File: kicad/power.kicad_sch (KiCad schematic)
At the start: 65 parts, among them J9 USB_C_Receptacle_USB2.0_16P, SW15 PH_IND, T1 475uH, U20 TPS7A39, U21 SN6505BDBV, U22 TPS2116DRL, U23 TPS62172DSG, U25 TPS7A2009, U26 TPS62171DSG, U27 TPS7A4101, U28 TPS61391, U29 CH224K

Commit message: layout updates
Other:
- note added: "power supply"
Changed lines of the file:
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@@
+		)
+	)
+	(text "power supply"
+		(exclude_from_sim no)
+		(at 352.806 245.872 0)
+		(effects
+			(font
+				(size 2.54 2.54)
+			)
+			(justify left bottom)
 		)
 	)

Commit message: #16
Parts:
- C172, C173: value 0.47uF -> 470nF
- C176: value 0.01uF -> 10nF
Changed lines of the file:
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@@
 			)
 		)
-		(property "Value" "0.47uF"
+		(property "Value" "470nF"
 			(at 105.41 204.4699 0)
 			(show_name no)
@@
 			)
 		)
-		(property "Value" "0.01uF"
+		(property "Value" "10nF"
 			(at 196.85 204.4699 0)
 			(show_name no)
@@
 			)
 		)
-		(property "Value" "0.47uF"
+		(property "Value" "470nF"
 			(at 91.44 204.4699 0)
 			(show_name no)

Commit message: power supply footprints
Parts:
- removed C164: 10uF, symbol Device:C
- removed D60, D61: D_Schottky, symbol Device:D_Schottky
- removed D62: 100V, symbol Device:D
- added D61: BAS316, Diode_SMD:D_SOD-323, symbol Diode:BAS316
- added D64, D69: MBR0580, Diode_SMD:D_SOD-123, symbol Diode:MBR0580
- C157, C158, C159, C160, C161, C162, C165, C166, C167, C168, C169, C170, C171, C172, C173, C174, C175, C176, C177, C178, C180, C197, C198: footprint (none) -> Capacitor_SMD:C_0805_2012Metric_Pad1.18x1.45mm_HandSolder
- C163: value 10uF -> 22uF; footprint (none) -> Capacitor_SMD:C_0805_2012Metric_Pad1.18x1.45mm_HandSolder
- C179: footprint (none) -> Capacitor_SMD:C_0603_1608Metric_Pad1.08x0.95mm_HandSolder
- D63: footprint (none) -> LED_SMD:LED_0603_1608Metric_Pad1.05x0.95mm_HandSolder
- R103, R104, R105, R106, R107, R108, R109, R112, R113, R114, R115, R118, R119, R120, R121, R122: footprint (none) -> Resistor_SMD:R_0805_2012Metric_Pad1.20x1.40mm_HandSolder
- R110: value 10k -> 330k; footprint (none) -> Resistor_SMD:R_0805_2012Metric_Pad1.20x1.40mm_HandSolder
- R111: value 10k -> 100k; footprint (none) -> Resistor_SMD:R_0805_2012Metric_Pad1.20x1.40mm_HandSolder
- R116, R117: footprint (none) -> Resistor_SMD:R_0603_1608Metric_Pad0.98x0.95mm_HandSolder
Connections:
- net at C172.1, C173.1, C174.1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: now also D61.1 (K)
- net at L3.2, U28.8 (SW): now also D61.2 (A)
- net at C162.2, U20.5 (INN): now also D69.2 (A)
- net at C158.1, R105.1, U20.1 (INP): now also D64.1 (K)
- net at T1.6: now also D64.2 (A), D69.1 (K)
- net GND1 renamed GNDA

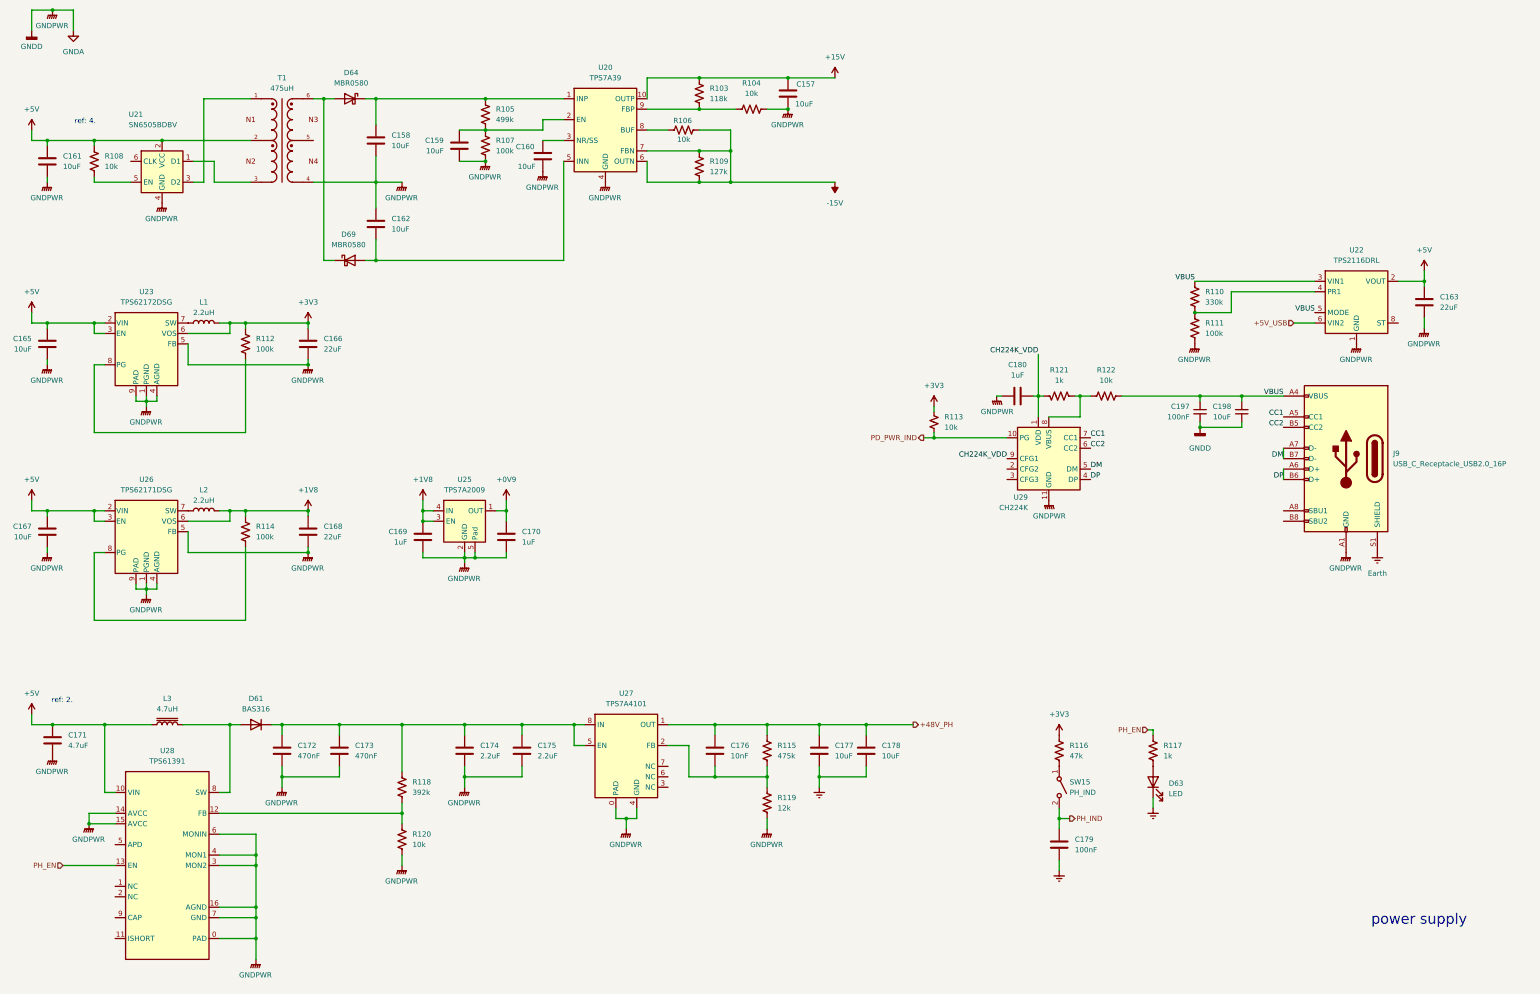
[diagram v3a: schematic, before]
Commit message: push buttons
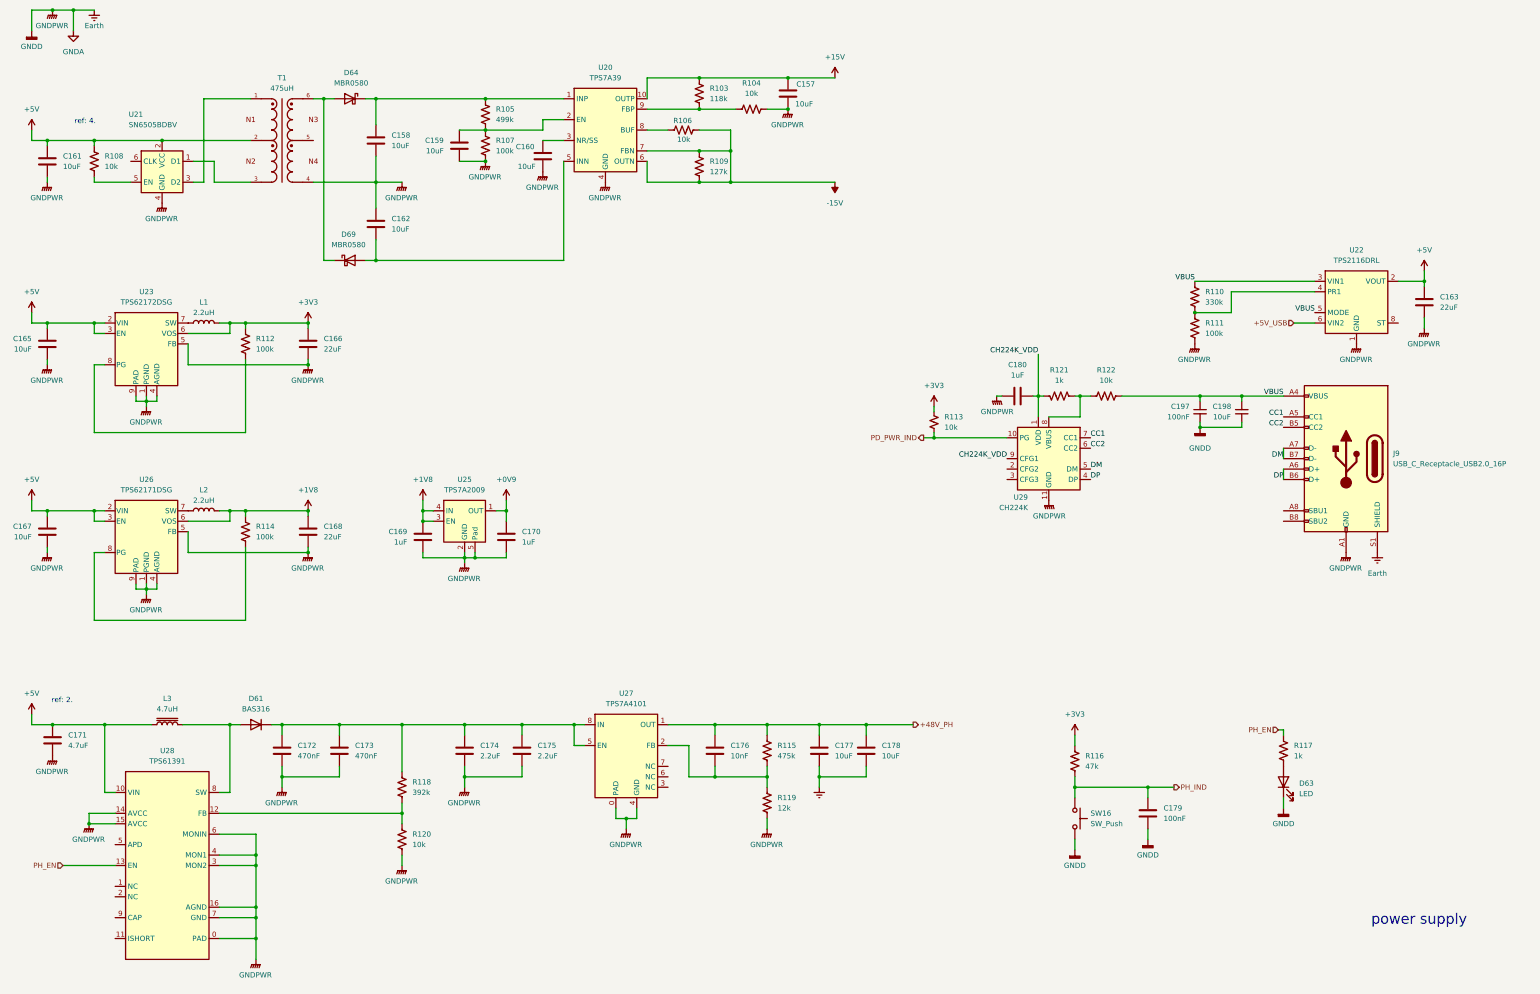
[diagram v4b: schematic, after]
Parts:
- removed SW15: PH_IND, symbol Switch:SW_SPST
- added SW16: SW_Push, Button_Switch_SMD:SW_Push_1P1T_XKB_TS-1187A, symbol Switch:SW_Push
- J9: footprint (none) -> Connector_USB:USB_C_Receptacle_HRO_TYPE-C-31-M-12
- T1: footprint WE-PPTI_1006:WE-PPTI_1006_L10.2W6.73H4.19 -> openmic:Wurth Elektronik 760390015
- U27: footprint (none) -> Package_SO:Texas_DGN0008B_VSSOP-8-1EP_3x3mm_P0.65mm_EP2x3mm_Mask1.88x1.98mm_ThermalVias
- U28: footprint (none) -> openmic:TPS61391
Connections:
- net GNDA is gone; now on net Earth: C157.2, C158.2, C159.2, C160.2, C161.2, C162.1, C163.2, C165.2, C166.2, C167.2, C168.2, C169.2, C170.2, C171.2, C172.2, C173.2, C174.2, C175.2, C180.2, C197.2, C198.1, J9.A1 (GND), J9.A12 (GND), J9.B1 (GND), J9.B12 (GND), R104.2, R107.2, R111.2, R119.2, R120.2, T1.4, U20.11 (GND), U20.4 (GND), U21.4 (GND), U22.1 (GND), U23.1 (PGND), U23.4 (AGND), U23.5 (FB), U23.9 (PAD), U25.2 (GND), U25.5 (Pad), U26.1 (PGND), U26.4 (AGND), U26.5 (FB), U26.9 (PAD), U27.0 (PAD), U27.4 (GND), U28.0 (PAD), U28.14 (AVCC), U28.15 (AVCC), U28.16 (AGND), U28.3 (MON2), U28.4 (MON1), U28.6 (MONIN), U28.7 (GND), U29.11 (GND)
- net Earth: now also SW16.2
- net PH_IND: now also R116.2, SW16.1
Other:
- moved on the sheet: D63, R117

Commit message: footprint selection
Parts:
- L1, L2, L3: footprint (none) -> Inductor_SMD:L_Wuerth_PMCI-201610
- R113: footprint Resistor_SMD:R_0805_2012Metric_Pad1.20x1.40mm_HandSolder -> Resistor_SMD:R_0603_1608Metric_Pad0.98x0.95mm_HandSolder

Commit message: footprints
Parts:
- U28: footprint openmic:TPS61391 -> Package_DFN_QFN:WQFN-16-1EP_3x3mm_P0.5mm_EP1.6x1.6mm
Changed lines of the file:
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@@
 			)
 		)
-		(property "Footprint" "openmic:TPS61391"
+		(property "Footprint" "Package_DFN_QFN:WQFN-16-1EP_3x3mm_P0.5mm_EP1.6x1.6mm"
 			(at 59.69 231.14 0)
 			(hide yes)

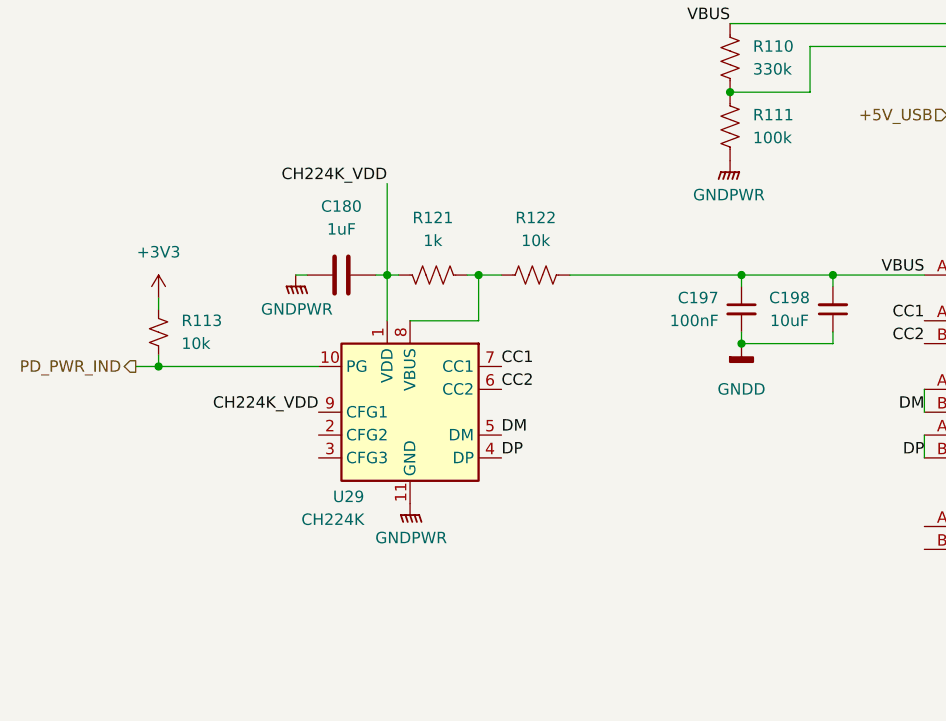
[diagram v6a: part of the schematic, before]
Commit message: update ch224k vdd
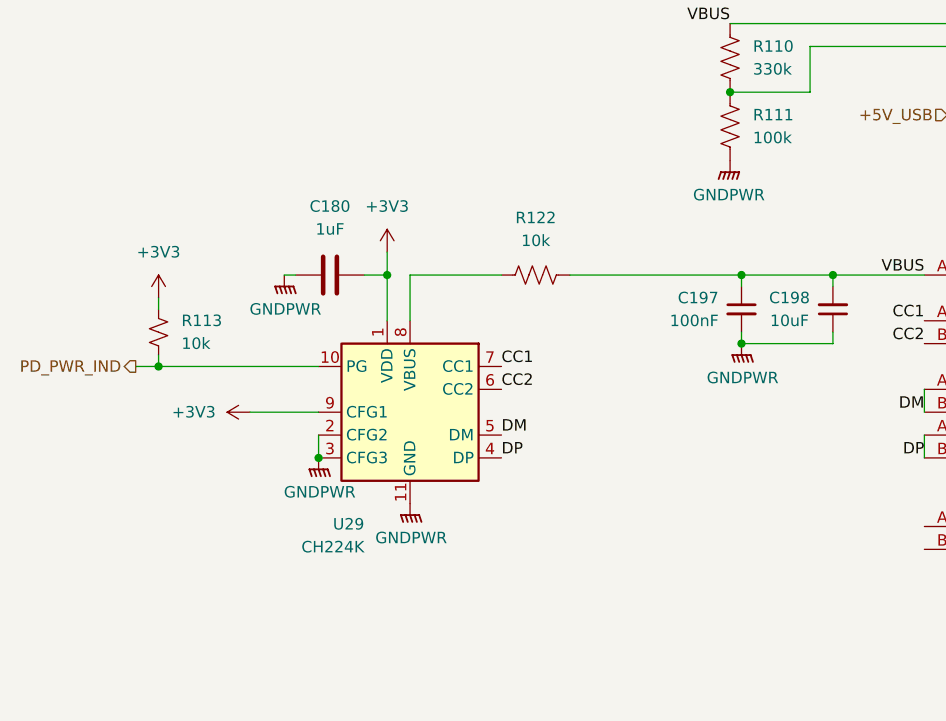
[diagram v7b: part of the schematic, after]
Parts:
- removed R121: 1k, Resistor_SMD:R_0805_2012Metric_Pad1.20x1.40mm_HandSolder, symbol Device:R_US
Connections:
- net CH224K_VDD is gone; now on net +3V3: C180.1, U29.1 (VDD), U29.9 (CFG1)
- net Earth: now also U29.2 (CFG2), U29.3 (CFG3)
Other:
- moved on the sheet: C180

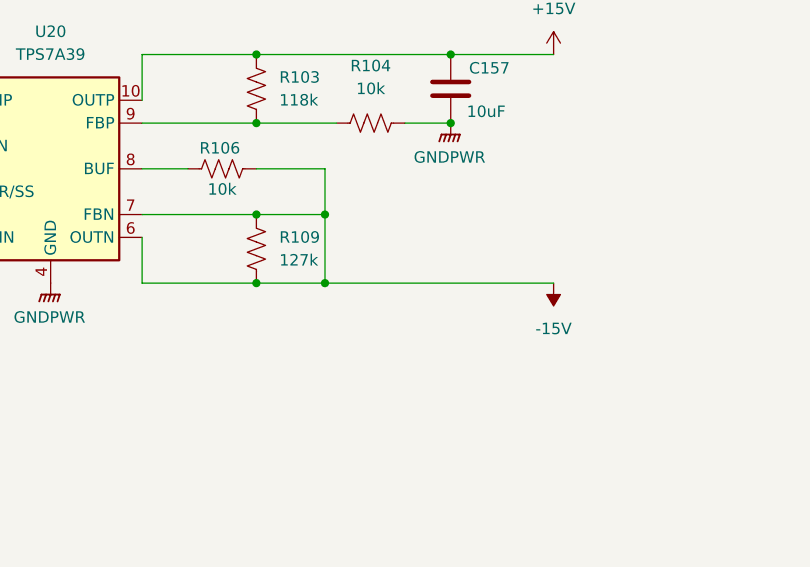
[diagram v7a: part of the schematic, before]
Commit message: +/-15V supply output
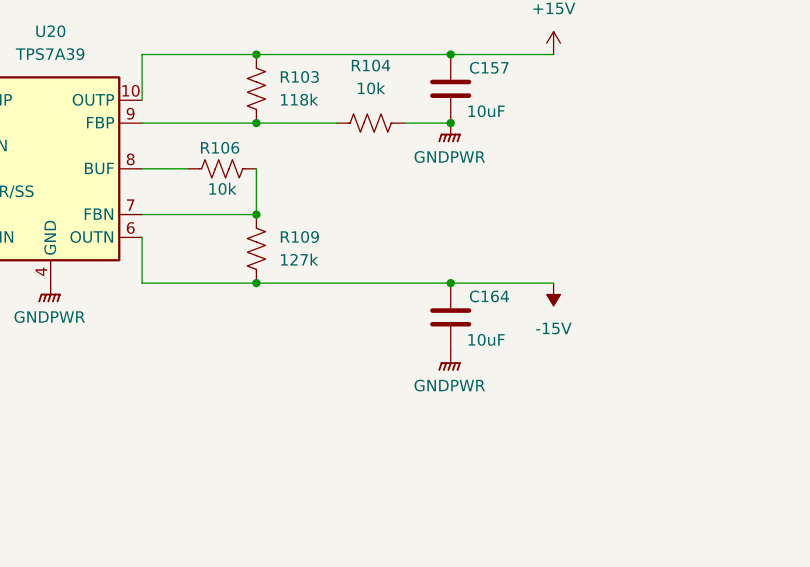
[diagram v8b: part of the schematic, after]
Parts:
- added C164: 10uF, Capacitor_SMD:C_0805_2012Metric_Pad1.18x1.45mm_HandSolder, symbol Device:C
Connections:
- net -15V: now also C164.1; no longer R106.2, R109.1, U20.7 (FBN)
- net Earth: now also C164.2
- new net: R106.2, R109.1, U20.7 (FBN)
